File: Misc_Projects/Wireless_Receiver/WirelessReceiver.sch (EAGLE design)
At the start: 10 parts, among them Q1 600mA/40V, Q2 600mA/40V, Q3 600mA/40V, X2 JST-XH-06-PIN-LONG-PAD

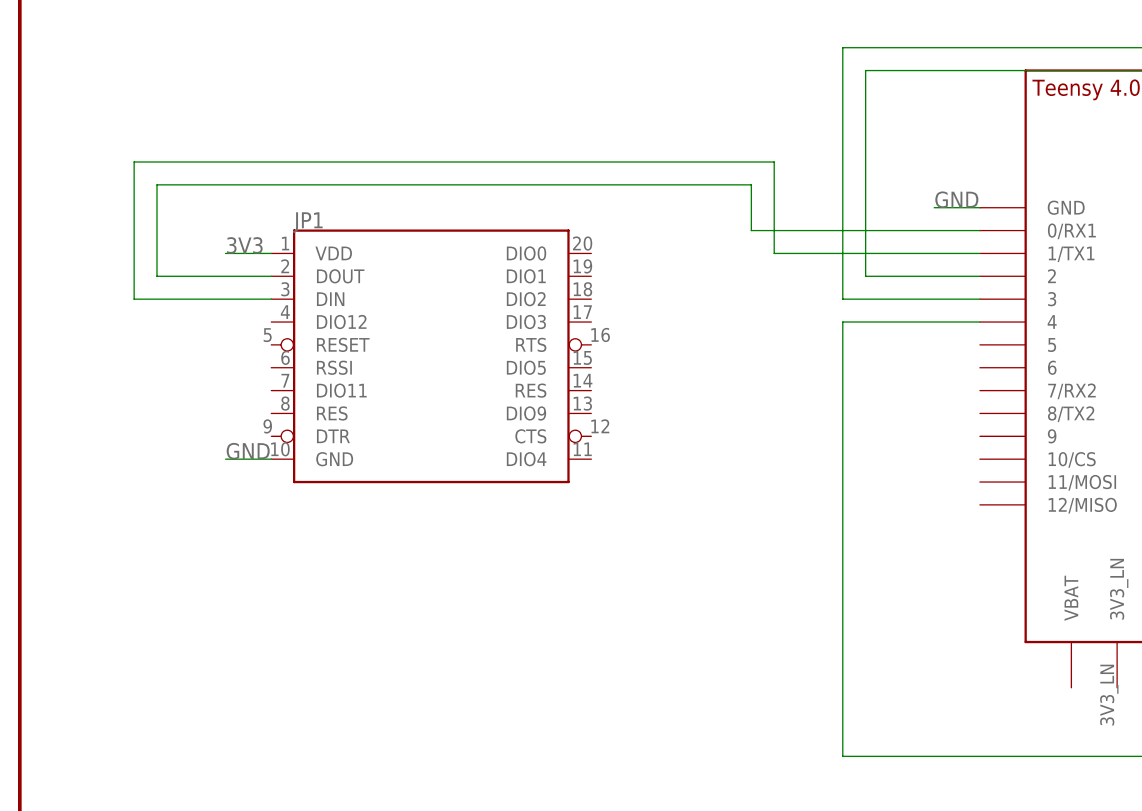
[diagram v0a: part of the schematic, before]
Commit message: Changed Wireless Receiver Xbee 3 Pro to Xbee Pro S3B
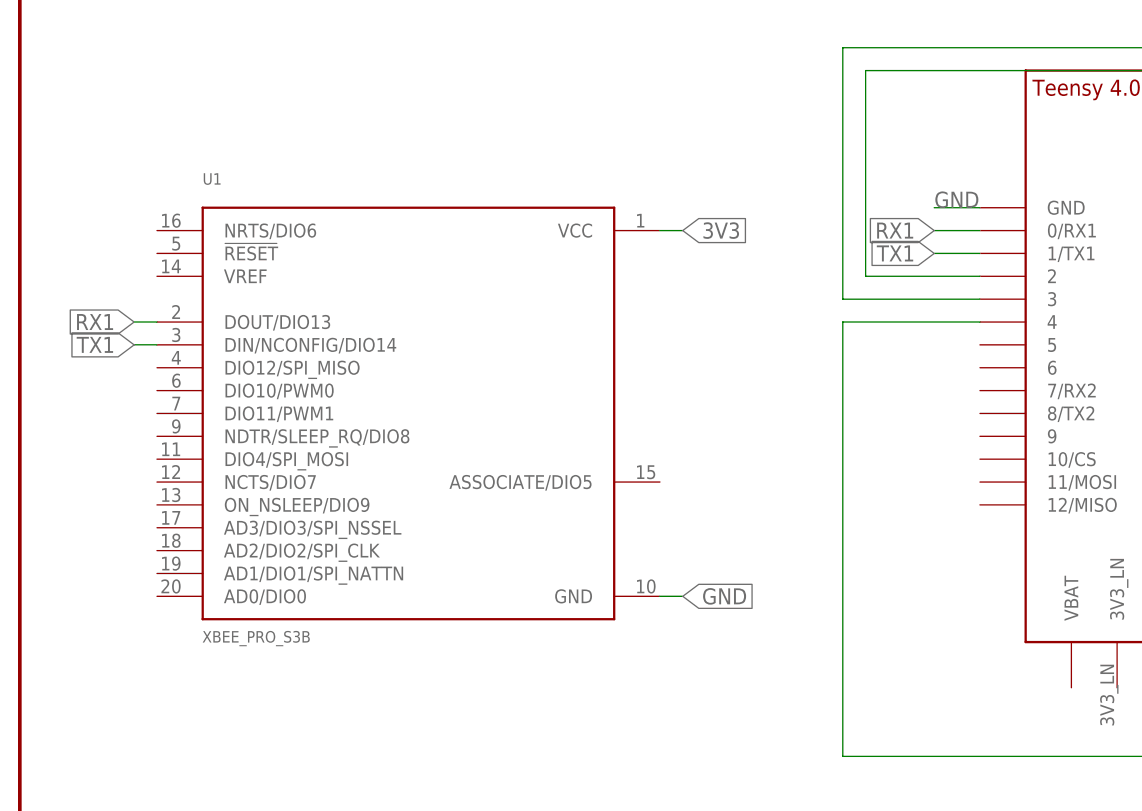
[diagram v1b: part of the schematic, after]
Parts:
- removed JP1: (no value), SparkFun-RF:XBEE
- added U1: XBEE_PRO_S3B, GTOR - Microcontroller:XBEE_PRO_S3B
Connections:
- removed net N$1: JP1.DOUT, U$1.0/RX1
- removed net N$2: JP1.DIN, U$1.1/TX1
- new net RX1: U$1.0/RX1, U1.DOUT/DIO13
- new net TX1: U$1.1/TX1, U1.DIN/NCONFIG/DIO14
- net 3V3: now also U1.VCC; no longer JP1.VDD
- net GND: now also U1.GND; no longer JP1.GND
